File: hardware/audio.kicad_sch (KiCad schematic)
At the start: 5 parts, among them J10 AudioJack_PJ-342

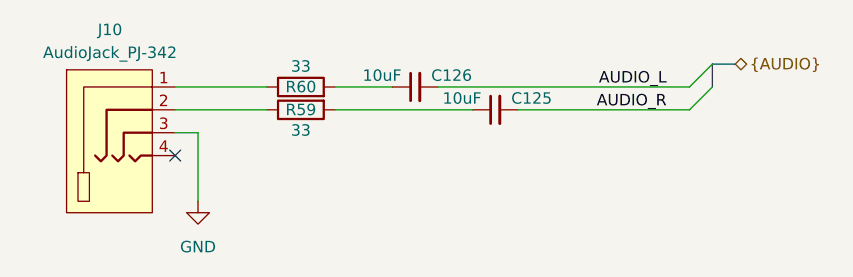
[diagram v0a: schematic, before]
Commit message: Update crystal
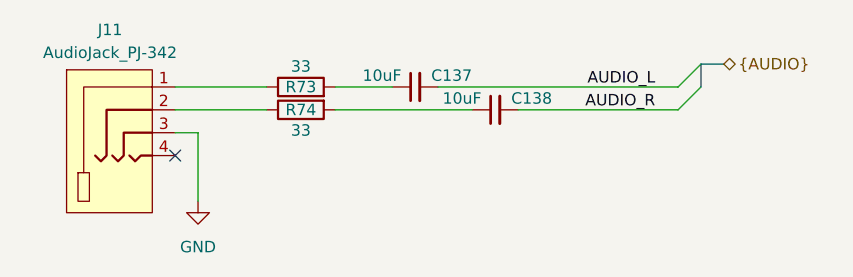
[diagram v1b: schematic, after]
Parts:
- renumbered C126 to C137, C125 to C138, J10 to J11, R60 to R73, R59 to R74
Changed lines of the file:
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@@
 	)
 	(bus_entry
-		(at 189.23 90.17)
+		(at 187.96 90.17)
 		(size 2.54 -2.54)
 		(stroke
@@
 	)
 	(bus_entry
-		(at 189.23 87.63)
+		(at 187.96 87.63)
 		(size 2.54 -2.54)
 		(stroke
@@
 	(wire
 		(pts
-			(xy 161.29 87.63) (xy 189.23 87.63)
+			(xy 161.29 87.63) (xy 187.96 87.63)
 		)
 		(stroke
@@
 	(bus
 		(pts
-			(xy 191.77 85.09) (xy 194.31 85.09)
+			(xy 190.5 85.09) (xy 193.04 85.09)
 		)
 		(stroke
@@
 	(wire
 		(pts
-			(xy 170.18 90.17) (xy 189.23 90.17)
+			(xy 170.18 90.17) (xy 187.96 90.17)
 		)
 		(stroke
@@
 	(bus
 		(pts
-			(xy 191.77 87.63) (xy 191.77 85.09)
+			(xy 190.5 87.63) (xy 190.5 85.09)
 		)
 		(stroke
@@
 	)
 	(label "AUDIO_L"
-		(at 186.69 87.63 180)
+		(at 185.42 87.63 180)
 		(effects
 			(font
@@
 	)
 	(label "AUDIO_R"
-		(at 186.69 90.17 180)
+		(at 185.42 90.17 180)
 		(effects
 			(font
@@
 	(hierarchical_label "{AUDIO}"
 		(shape bidirectional)
-		(at 194.31 85.09 0)
+		(at 193.04 85.09 0)
 		(effects
 			(font
@@
 		(on_board yes)
 		(dnp no)
-		(property "Reference" "R60"
+		(property "Reference" "R73"
 			(at 146.05 87.63 90)
 			(effects
@@
 			(project "cm0"
 				(path "/b53f5dbb-8078-4818-9e8f-fdf90ba6d854/5ae223d4-d68f-4671-997c-b9179dc72885"
-					(reference "R60")
+					(reference "R73")
 					(unit 1)
 				)
@@
 		(dnp no)
 		(fields_autoplaced yes)
-		(property "Reference" "J10"
+		(property "Reference" "J11"
 			(at 124.841 81.28 0)
 			(effects
@@
 			(project ""
 				(path "/b53f5dbb-8078-4818-9e8f-fdf90ba6d854/5ae223d4-d68f-4671-997c-b9179dc72885"
-					(reference "J10")
+					(reference "J11")
 					(unit 1)
 				)
@@
 		(on_board yes)
 		(dnp no)
-		(property "Reference" "C125"
+		(property "Reference" "C138"
 			(at 169.418 88.9 90)
 			(effects
@@
 			(project "cm0"
 				(path "/b53f5dbb-8078-4818-9e8f-fdf90ba6d854/5ae223d4-d68f-4671-997c-b9179dc72885"
-					(reference "C125")
+					(reference "C138")
 					(unit 1)
 				)
@@
 		(on_board yes)
 		(dnp no)
-		(property "Reference" "R59"
+		(property "Reference" "R74"
 			(at 146.05 90.17 90)
 			(effects
@@
 			(project "cm0"
 				(path "/b53f5dbb-8078-4818-9e8f-fdf90ba6d854/5ae223d4-d68f-4671-997c-b9179dc72885"
-					(reference "R59")
+					(reference "R74")
 					(unit 1)
 				)
@@
 		(on_board yes)
 		(dnp no)
-		(property "Reference" "C126"
+		(property "Reference" "C137"
 			(at 160.528 86.36 90)
 			(effects
@@
 			(project "cm0"
 				(path "/b53f5dbb-8078-4818-9e8f-fdf90ba6d854/5ae223d4-d68f-4671-997c-b9179dc72885"
-					(reference "C126")
+					(reference "C137")
 					(unit 1)
 				)
@@
 		(dnp no)
 		(fields_autoplaced yes)
-		(property "Reference" "#PWR0156"
+		(property "Reference" "#PWR0190"
 			(at 134.62 106.68 0)
 			(effects
@@
 			(project ""
 				(path "/b53f5dbb-8078-4818-9e8f-fdf90ba6d854/5ae223d4-d68f-4671-997c-b9179dc72885"
-					(reference "#PWR0156")
+					(reference "#PWR0190")
 					(unit 1)
 				)

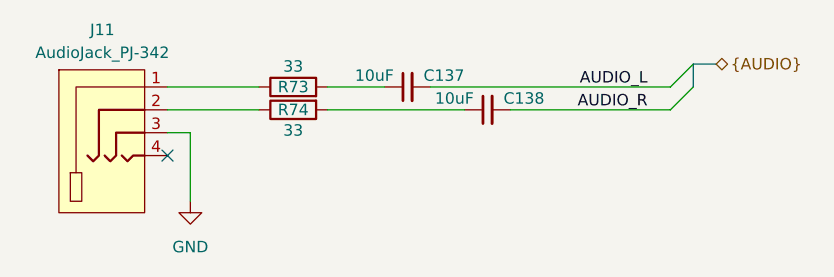
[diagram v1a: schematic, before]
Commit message: Updated README and improved audio routing
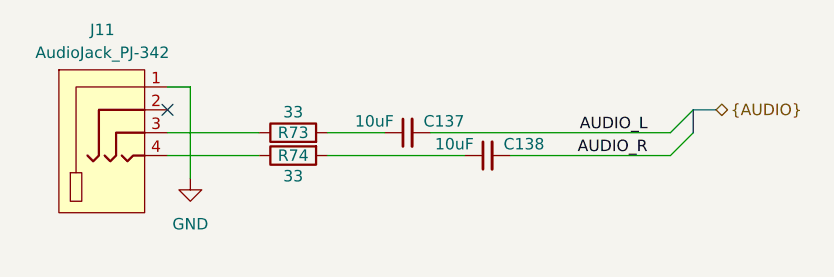
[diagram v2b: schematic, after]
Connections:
- net GND: now also J11.1; no longer J11.3
- net at R73.1: now also J11.3; no longer J11.1
- net at J11.2: no longer R74.1
- net at J11.4: now also R74.1
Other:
- moved on the sheet: C137, C138, R73, R74
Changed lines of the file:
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@@
 	)
 	(no_connect
-		(at 132.08 95.25)
+		(at 132.08 90.17)
 	)
 	(bus_entry
-		(at 187.96 90.17)
+		(at 187.96 95.25)
 		(size 2.54 -2.54)
 		(stroke
@@
 	)
 	(bus_entry
-		(at 187.96 87.63)
+		(at 187.96 92.71)
 		(size 2.54 -2.54)
 		(stroke
@@
 	(wire
 		(pts
-			(xy 132.08 87.63) (xy 142.24 87.63)
+			(xy 132.08 92.71) (xy 142.24 92.71)
 		)
 		(stroke
@@
 	(wire
 		(pts
-			(xy 161.29 87.63) (xy 187.96 87.63)
+			(xy 161.29 92.71) (xy 187.96 92.71)
 		)
 		(stroke
@@
 	(wire
 		(pts
-			(xy 149.86 90.17) (xy 165.1 90.17)
+			(xy 149.86 95.25) (xy 165.1 95.25)
 		)
 		(stroke
@@
 	(wire
 		(pts
-			(xy 134.62 100.33) (xy 134.62 92.71)
+			(xy 134.62 87.63) (xy 134.62 97.79)
 		)
 		(stroke
@@
 	(wire
 		(pts
-			(xy 149.86 87.63) (xy 156.21 87.63)
+			(xy 149.86 92.71) (xy 156.21 92.71)
 		)
 		(stroke
@@
 	(bus
 		(pts
-			(xy 190.5 85.09) (xy 193.04 85.09)
+			(xy 190.5 90.17) (xy 193.04 90.17)
 		)
 		(stroke
@@
 	(wire
 		(pts
-			(xy 170.18 90.17) (xy 187.96 90.17)
+			(xy 170.18 95.25) (xy 187.96 95.25)
 		)
 		(stroke
@@
 	(wire
 		(pts
-			(xy 134.62 92.71) (xy 132.08 92.71)
+			(xy 134.62 87.63) (xy 132.08 87.63)
 		)
 		(stroke
@@
 	(bus
 		(pts
-			(xy 190.5 87.63) (xy 190.5 85.09)
+			(xy 190.5 92.71) (xy 190.5 90.17)
 		)
 		(stroke
@@
 	(wire
 		(pts
-			(xy 132.08 90.17) (xy 142.24 90.17)
+			(xy 132.08 95.25) (xy 142.24 95.25)
 		)
 		(stroke
@@
 	)
 	(label "AUDIO_L"
-		(at 185.42 87.63 180)
+		(at 185.42 92.71 180)
 		(effects
 			(font
@@
 	)
 	(label "AUDIO_R"
-		(at 185.42 90.17 180)
+		(at 185.42 95.25 180)
 		(effects
 			(font
@@
 	(hierarchical_label "{AUDIO}"
 		(shape bidirectional)
-		(at 193.04 85.09 0)
+		(at 193.04 90.17 0)
 		(effects
 			(font
@@
 	(symbol
 		(lib_id "Device:R")
-		(at 146.05 87.63 90)
+		(at 146.05 92.71 90)
 		(unit 1)
 		(exclude_from_sim no)
@@
 		(dnp no)
 		(property "Reference" "R73"
-			(at 146.05 87.63 90)
+			(at 146.05 92.71 90)
 			(effects
 				(font
@@
 		)
 		(property "Value" "33"
-			(at 146.05 85.344 90)
+			(at 146.05 90.424 90)
 			(effects
 				(font
@@
 		)
 		(property "Footprint" "Resistor_SMD:R_0402_1005Metric"
-			(at 146.05 89.408 90)
+			(at 146.05 94.488 90)
 			(effects
 				(font
@@
 		)
 		(property "Datasheet" "~"
-			(at 146.05 87.63 0)
+			(at 146.05 92.71 0)
 			(effects
 				(font
@@
 		)
 		(property "Description" "Resistor"
-			(at 146.05 87.63 0)
+			(at 146.05 92.71 0)
 			(effects
 				(font
@@
 		)
 		(property "LCSC Part #" "C25105"
-			(at 146.05 87.63 90)
+			(at 146.05 92.71 90)
 			(effects
 				(font
@@
 		)
 		(property "FT Position Offset" ""
-			(at 146.05 87.63 90)
+			(at 146.05 92.71 90)
 			(effects
 				(font
@@
 		)
 		(property "FT Rotation Offset" ""
-			(at 146.05 87.63 90)
+			(at 146.05 92.71 90)
 			(effects
 				(font
@@
 	(symbol
 		(lib_id "Device:C_Small")
-		(at 167.64 90.17 90)
+		(at 167.64 95.25 90)
 		(unit 1)
 		(exclude_from_sim no)
@@
 		(dnp no)
 		(property "Reference" "C138"
-			(at 169.418 88.9 90)
+			(at 169.418 93.98 90)
 			(effects
 				(font
@@
 		)
 		(property "Value" "10uF"
-			(at 166.116 88.9 90)
+			(at 166.116 93.98 90)
 			(effects
 				(font
@@
 		)
 		(property "Footprint" "Capacitor_SMD:C_0603_1608Metric"
-			(at 167.64 90.17 0)
+			(at 167.64 95.25 0)
 			(effects
 				(font
@@
 		)
 		(property "Datasheet" "~"
-			(at 167.64 90.17 0)
+			(at 167.64 95.25 0)
 			(effects
 				(font
@@
 		)
 		(property "Description" "Unpolarized capacitor, small symbol"
-			(at 167.64 90.17 0)
+			(at 167.64 95.25 0)
 			(effects
 				(font
@@
 		)
 		(property "LCSC Part #" "C19702"
-			(at 167.64 90.17 0)
+			(at 167.64 95.25 0)
 			(effects
 				(font
@@
 		)
 		(property "FT Position Offset" ""
-			(at 167.64 90.17 90)
+			(at 167.64 95.25 90)
 			(effects
 				(font
@@
 		)
 		(property "FT Rotation Offset" ""
-			(at 167.64 90.17 90)
+			(at 167.64 95.25 90)
 			(effects
 				(font
@@
 	(symbol
 		(lib_id "Device:R")
-		(at 146.05 90.17 90)
+		(at 146.05 95.25 90)
 		(mirror x)
 		(unit 1)
@@
 		(dnp no)
 		(property "Reference" "R74"
-			(at 146.05 90.17 90)
+			(at 146.05 95.25 90)
 			(effects
 				(font
@@
 		)
 		(property "Value" "33"
-			(at 146.05 92.456 90)
+			(at 146.05 97.536 90)
 			(effects
 				(font
@@
 		)
 		(property "Footprint" "Resistor_SMD:R_0402_1005Metric"
-			(at 146.05 88.392 90)
+			(at 146.05 93.472 90)
 			(effects
 				(font
@@
 		)
 		(property "Datasheet" "~"
-			(at 146.05 90.17 0)
+			(at 146.05 95.25 0)
 			(effects
 				(font
@@
 		)
 		(property "Description" "Resistor"
-			(at 146.05 90.17 0)
+			(at 146.05 95.25 0)
 			(effects
 				(font
@@
 		)
 		(property "LCSC Part #" "C25105"
-			(at 146.05 90.17 90)
+			(at 146.05 95.25 90)
 			(effects
 				(font
@@
 		)
 		(property "FT Position Offset" ""
-			(at 146.05 90.17 90)
+			(at 146.05 95.25 90)
 			(effects
 				(font
@@
 		)
 		(property "FT Rotation Offset" ""
-			(at 146.05 90.17 90)
+			(at 146.05 95.25 90)
 			(effects
 				(font
@@
 	(symbol
 		(lib_id "Device:C_Small")
-		(at 158.75 87.63 90)
+		(at 158.75 92.71 90)
 		(unit 1)
 		(exclude_from_sim no)
@@
 		(dnp no)
 		(property "Reference" "C137"
-			(at 160.528 86.36 90)
+			(at 160.528 91.44 90)
 			(effects
 				(font
@@
 		)
 		(property "Value" "10uF"
-			(at 157.226 86.36 90)
+			(at 157.226 91.44 90)
 			(effects
 				(font
@@
 		)
 		(property "Footprint" "Capacitor_SMD:C_0603_1608Metric"
-			(at 158.75 87.63 0)
+			(at 158.75 92.71 0)
 			(effects
 				(font
@@
 		)
 		(property "Datasheet" "~"
-			(at 158.75 87.63 0)
+			(at 158.75 92.71 0)
 			(effects
 				(font
@@
 		)
 		(property "Description" "Unpolarized capacitor, small symbol"
-			(at 158.75 87.63 0)
+			(at 158.75 92.71 0)
 			(effects
 				(font
@@
 		)
 		(property "LCSC Part #" "C19702"
-			(at 158.75 87.63 0)
+			(at 158.75 92.71 0)
 			(effects
 				(font
@@
 		)
 		(property "FT Position Offset" ""
-			(at 158.75 87.63 90)
+			(at 158.75 92.71 90)
 			(effects
 				(font
@@
 		)
 		(property "FT Rotation Offset" ""
-			(at 158.75 87.63 90)
+			(at 158.75 92.71 90)
 			(effects
 				(font
@@
 	(symbol
 		(lib_id "power:GND")
-		(at 134.62 100.33 0)
+		(at 134.62 97.79 0)
 		(unit 1)
 		(exclude_from_sim no)
@@
 		(fields_autoplaced yes)
 		(property "Reference" "#PWR0190"
-			(at 134.62 106.68 0)
+			(at 134.62 104.14 0)
 			(effects
 				(font
@@
 		)
 		(property "Value" "GND"
-			(at 134.62 105.41 0)
+			(at 134.62 102.87 0)
 			(effects
 				(font
@@
 		)
 		(property "Footprint" ""
-			(at 134.62 100.33 0)
+			(at 134.62 97.79 0)
 			(effects
 				(font
@@
 		)
 		(property "Datasheet" ""
-			(at 134.62 100.33 0)
+			(at 134.62 97.79 0)
 			(effects
 				(font
@@
 		)
 		(property "Description" "Power symbol creates a global label with name \"GND\" , ground"
-			(at 134.62 100.33 0)
-			(effects
-				(font
+			(at 134.62 97.79 0)
+			(effects
+				(font

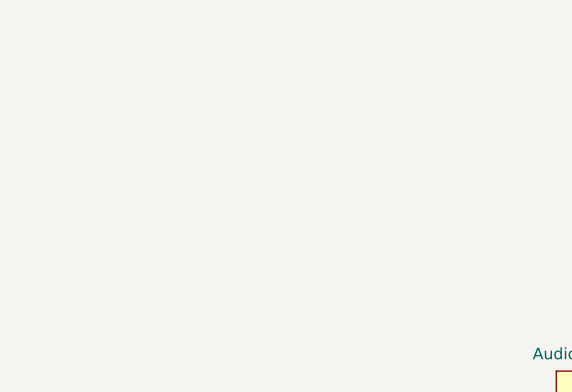
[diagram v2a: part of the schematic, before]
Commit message: Add schematic pdf
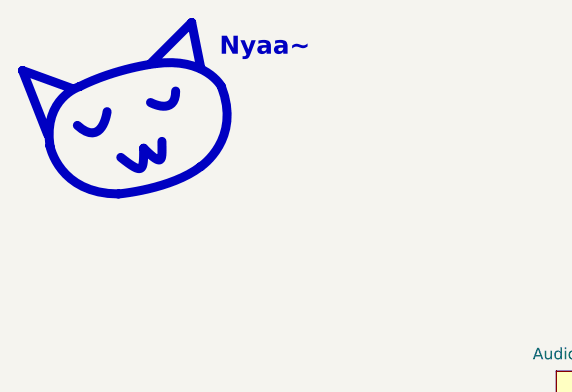
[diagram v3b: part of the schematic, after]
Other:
- note added: "Nyaa~"
- title: Icepi CM0 -> Icepi SBC
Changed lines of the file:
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@@
 	(paper "A4")
 	(title_block
-		(title "Icepi CM0")
-		(date "2025-11-21")
+		(title "Icepi SBC")
+		(date "2025-12-21")
 		(rev "v1.0")
 		(company "Icy Electronics")
 		(comment 1 "Chengyin Yao (cheyao)")
-		(comment 2 "https://github.com/cheyao/icepi-cm0")
+		(comment 2 "https://github.com/cheyao/icepi-sbc")
 		(comment 3 "License: Solderpad")
 	)
+	(bezier
+		(pts
+			(xy 63.754 60.706) (xy 62.992 55.372) (xy 67.056 54.102) (xy 67.056 54.102)
+		)
+		(stroke
+			(width 1)
+			(type default)
+		)
+		(fill
+			(type none)
+		)
+	)
+	(bezier
+		(pts
+			(xy 74.168 60.96) (xy 76.454 63.246) (xy 76.2 62.23) (xy 76.2 60.198)
+		)
+		(stroke
+			(width 1)
+			(type default)
+		)
+		(fill
+			(type none)
+		)
+	)
+	(bezier
+		(pts
+			(xy 80.518 62.992) (xy 77.216 65.532) (xy 71.374 66.04) (xy 71.374 66.04)
+		)
+		(stroke
+			(width 1)
+			(type default)
+		)
+		(fill
+			(type none)
+		)
+	)
+	(bezier
+		(pts
+			(xy 71.374 66.04) (xy 64.77 66.04) (xy 63.754 60.706) (xy 63.754 60.706)
+		)
+		(stroke
+			(width 1)
+			(type default)
+		)
+		(fill
+			(type none)
+		)
+	)
+	(bezier
+		(pts
+			(xy 74.93 51.562) (xy 74.93 51.562) (xy 79.502 46.99) (xy 79.502 46.99)
+		)
+		(stroke
+			(width 1)
+			(type default)
+		)
+		(fill
+			(type none)
+		)
+	)
+	(bezier
+		(pts
+			(xy 82.804 54.102) (xy 85.09 59.944) (xy 80.518 62.992) (xy 80.518 62.992)
+		)
+		(stroke
+			(width 1)
+			(type default)
+		)
+		(fill
+			(type none)
+		)
+	)
+	(bezier
+		(pts
+			(xy 71.628 61.976) (xy 74.168 64.008) (xy 74.168 63.5) (xy 74.168 60.96)
+		)
+		(stroke
+			(width 1)
+			(type default)
+		)
+		(fill
+			(type none)
+		)
+	)
+	(bezier
+		(pts
+			(xy 75.438 51.562) (xy 81.026 50.8) (xy 82.804 54.102) (xy 82.804 54.102)
+		)
+		(stroke
+			(width 1)
+			(type default)
+		)
+		(fill
+			(type none)
+		)
+	)
+	(bezier
+		(pts
+			(xy 66.802 58.42) (xy 69.596 60.96) (xy 70.104 56.896) (xy 70.104 56.896)
+		)
+		(stroke
+			(width 1)
+			(type default)
+		)
+		(fill
+			(type none)
+		)
+	)
+	(bezier
+		(pts
+			(xy 79.502 46.99) (xy 79.502 46.99) (xy 80.518 52.07) (xy 80.518 52.07)
+		)
+		(stroke
+			(width 1)
+			(type default)
+		)
+		(fill
+			(type none)
+		)
+	)
+	(bezier
+		(pts
+			(xy 66.294 54.356) (xy 66.294 54.356) (xy 60.706 52.324) (xy 60.706 52.324)
+		)
+		(stroke
+			(width 1)
+			(type default)
+		)
+		(fill
+			(type none)
+		)
+	)
+	(bezier
+		(pts
+			(xy 60.706 52.324) (xy 60.706 52.324) (xy 63.5 59.436) (xy 63.5 59.436)
+		)
+		(stroke
+			(width 1)
+			(type default)
+		)
+		(fill
+			(type none)
+		)
+	)
+	(bezier
+		(pts
+			(xy 67.056 54.102) (xy 71.12 52.07) (xy 75.438 51.562) (xy 75.438 51.562)
+		)
+		(stroke
+			(width 1)
+			(type default)
+		)
+		(fill
+			(type none)
+		)
+	)
+	(bezier
+		(pts
+			(xy 77.724 54.61) (xy 77.724 57.404) (xy 74.93 55.88) (xy 74.93 55.88)
+		)
+		(stroke
+			(width 1)
+			(type default)
+		)
+		(fill
+			(type none)
+		)
+	)
+	(text "Nyaa~"
+		(exclude_from_sim no)
+		(at 87.63 49.784 0)
+		(effects
+			(font
+				(size 2 2)
+				(thickness 0.4)
+				(bold yes)
+			)
+		)
+	)
 	(no_connect
